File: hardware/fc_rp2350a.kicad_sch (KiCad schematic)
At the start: 51 parts, among them Q1 AP1606, Q2 AP1606, U1 TS2306A 240GF MSM 9_C2976675, U2 RP2354A, X1 XTM25012000JT00351001

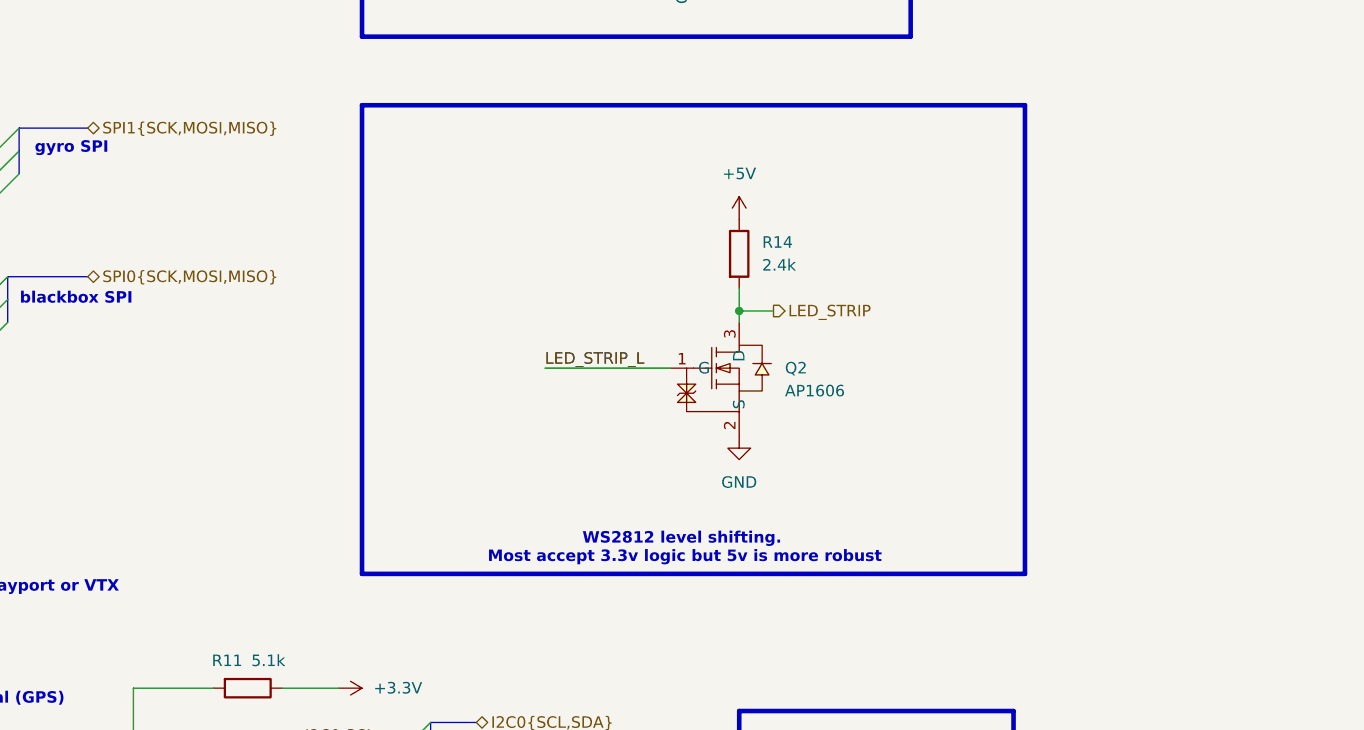
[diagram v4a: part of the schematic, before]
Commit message: LED strip: TXU0101 non-inverting stage replaces Q2/R14 (FB6 item 1, FW1)
Betaflight's RP2350 WS2812 driver cannot invert, so the inverting AP1606
open-drain stage (Q2 + R14 2.4k to +5V) is replaced by the OpenFC circuit:
GPIO8 /RP2354A/LED_STRIP_L -> U26 TXU0101DRYR (TI, SON-6 DRY) A -> BY ->
R115 200R 0201 (UNI-ROYAL 0201WMF2000TEE) -> LED_STRIP (LGA pad 46 ->
J20/J21/J31/J32). VCCA = Core +3.3V, VCCB = OE = +5V (as OpenFC U10; ds p19:
OE may be referenced to VCCA or VCCB, low/floating = Hi-Z). Bypass 100n
0201 GRM033R61E104KE14D on VCCA (C108) and VCCB (C109), ds p25.
Symbol, footprint and 3D model copied from ref-OpenFC into the project
libs (no silk; TI DRY0006A land; stencil 1:1 per ds p37 -> local paste
margin 0; courtyard on the body).

Core layout (F.Cu only, B.Cu still LGA only):
- U26 at the Q2/R14 slot (112.47,60.135) rot 270: A, GND and VCCA escape
  through three vias in the U2 removed-pad band (LED_STRIP_L In2, GND,
  +3.3V In3 plane); BY -> R115 below; R115 -> J91.46 via on F.
- C14 is 1.35 mm (pad edge) from VCCA, so C108 is kept, at the nearest
  legal spot: under R11, +3.3V pad on R11.1 (about 2 mm from U26).
- C109 right of R7 on the +5V feed (channel -> y61.5 -> C109 -> existing
  +5V track to via 117.65,60.2). R14's +5V via chain removed.
- Net-(R7-Pad1) now R7.1 -> via -> In2 -> existing via at U1 pin 2
  (that via was dangling before).
- U1 (BOOTSEL switch) 0.30 mm down; SCL pull-up stub rerouted along
  y59.37/x114.75; GND stitch via moved to 114.42,59.95; J50 'GND' label
  0.8 mm down (still beside J50) to clear C108.

DRC Core 28 -> 27 errors (via_dangling only), Base 21 unchanged; parity
non-missing 70/7 unchanged; unconnected 0/0; ERC 31 unchanged (warnings
+12: pin types as OpenFC symbol, 0201 nickname as existing parts).
Courtyard warnings Core 127 -> 132. Base board untouched.

Co-Authored-By: Claude Opus 5.5 <noreply@anthropic.com>
Claude-Session: https://claude.ai/code/session_01KTp3FLjVXfXdWrkmr6af7d
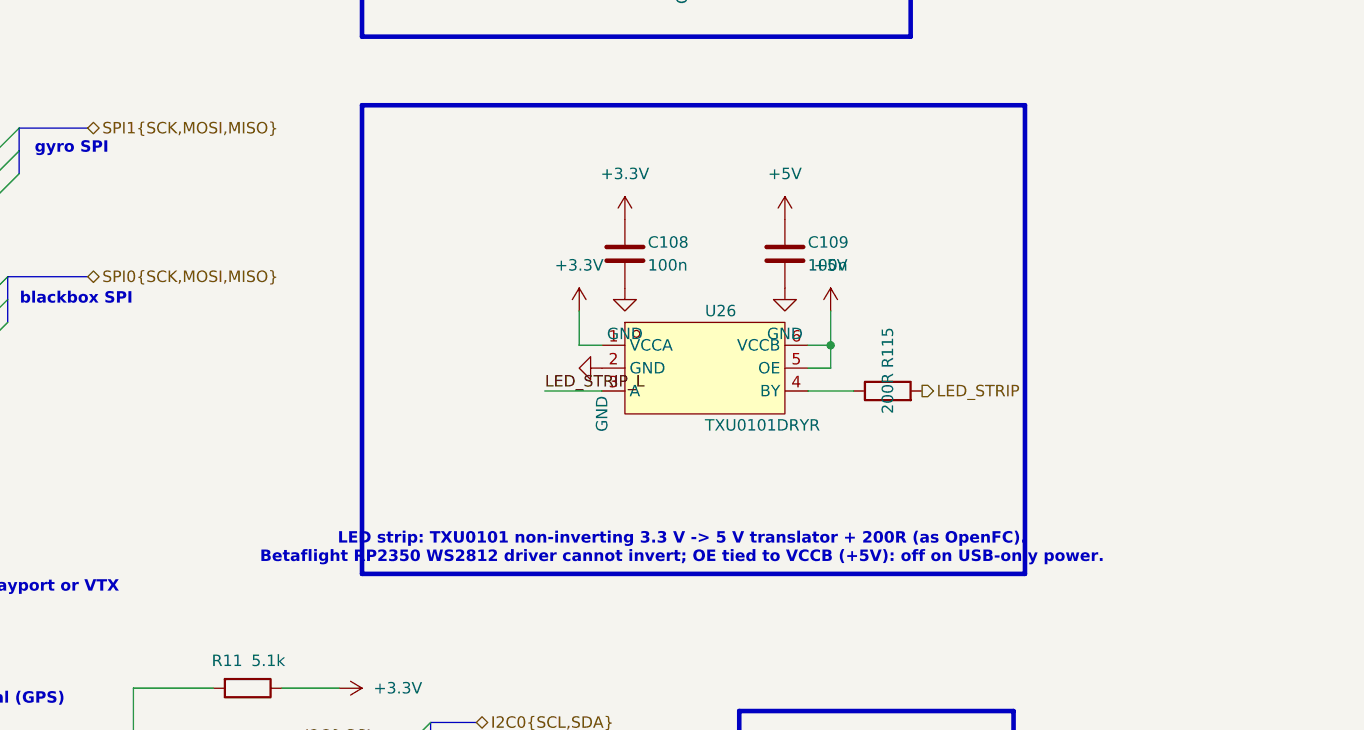
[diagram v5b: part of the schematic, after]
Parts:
- removed Q2: AP1606, lib:DFN-3L_L1.0-W0.6-P0.65-BR, symbol lib:DMN1150UFB-7B
- removed R14: 2.4k, Resistor_SMD:R_0201_0603Metric, symbol Device:R
- added C108, C109: 100n, Capacitor_SMD:C_0201_0603Metric, symbol Device:C
- added R115: 200R, Resistor_SMD:R_0201_0603Metric, symbol Device:R
- added U26: TXU0101DRYR, lib:SON-6_L1.5-W1.0-P0.50-TL, symbol lib:TXU0101DRYR
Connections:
- net +3.3V: now also C108.1, U26.1 (VCCA)
- net +5V: now also C109.1, U26.5 (OE), U26.6 (VCCB)
- net GND: now also C108.2, C109.2, U26.2 (GND)
- net LED_STRIP: now also R115.2
- net LED_STRIP_L: now also U26.3 (A)
- new net: R115.1, U26.4 (BY)
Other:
- note added: "LED strip: TXU0101 non-inverting 3.3 V -> 5 V translator + 200R (as OpenFC). Betaflight RP2350 WS2812 driver cannot invert; OE tied to VCCB (+5V): off on USB-only power."
- note removed: "WS2812 level shifting. Most accept 3.3v logic but 5v is more robust"

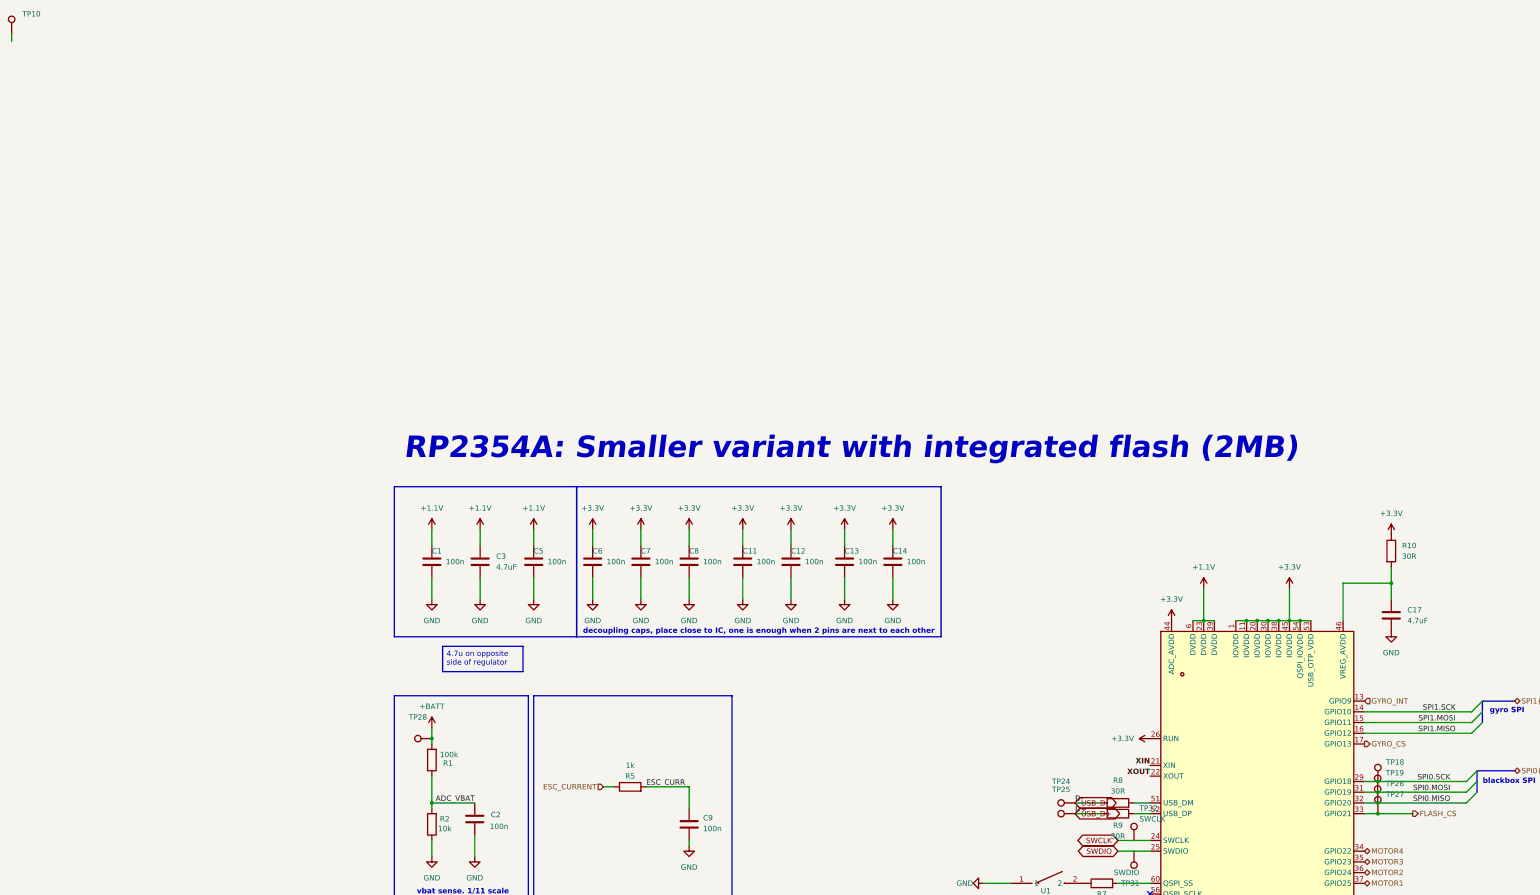
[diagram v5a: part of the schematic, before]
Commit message: One board: merge Base and Core onto the OpenAIO-Whoop 8L HDI stackup
- hardware/OpenAIO.kicad_pcb: the routed Base and Core layouts of 8fa8d7b
  side by side in one board, all routing kept (Core promoted to 8 layers
  before the append so no Base layer was dropped). J90/J91 LGA deleted;
  their 46 nets are now direct links (51 unconnected, listed in
  research/ROUTING.md). Stackup and board setup from OpenAIO-Whoop:
  8L HDI 1+6+1, 0.997 mm, 1 oz all layers, microvia 0.25/0.10,
  buried 0.33/0.15. Base DRC severities and exclusions kept.
- hardware/OpenAIO.kicad_dru: canonical block, Whoop HDI via rules,
  Base/Core rules that still apply; LGA, 2 oz and 1.6 mm via rules gone.
- Schematic: core_interface sheet removed; DPS368 baro U28 on I2C0;
  review fixes (U3 HF cap C116, RP2354 caps C117/C118, buzzer flyback D10,
  SD card on +3.3V, D9 on +4v5, FLASH_CS -> SD_CS, PWR_FLAGs, U7 pin
  names, ESC cap pin types, L4 LCSC). ERC 32 -> 0 errors.
- Libraries project-local: every footprint, 3D model and symbol in lib;
  OPENDRONE_LIB aliases removed from the lib tables.
- Two-board projects, multiboard config and LGA tools removed; Whoop
  board tools added in hardware/tools.
- Docs: README, AGENTS.md, research/ROUTING.md (hand-over),
  SCHEMATIC-REVIEW-2026-10-15.md, Betaflight target baro.

DRC: 38 errors (25 dangling LGA escape vias, 13 Core leftovers listed),
51 unconnected (the Base-Core links), 0 net or value parity issues.

Co-Authored-By: Claude Opus 5.5 <noreply@anthropic.com>
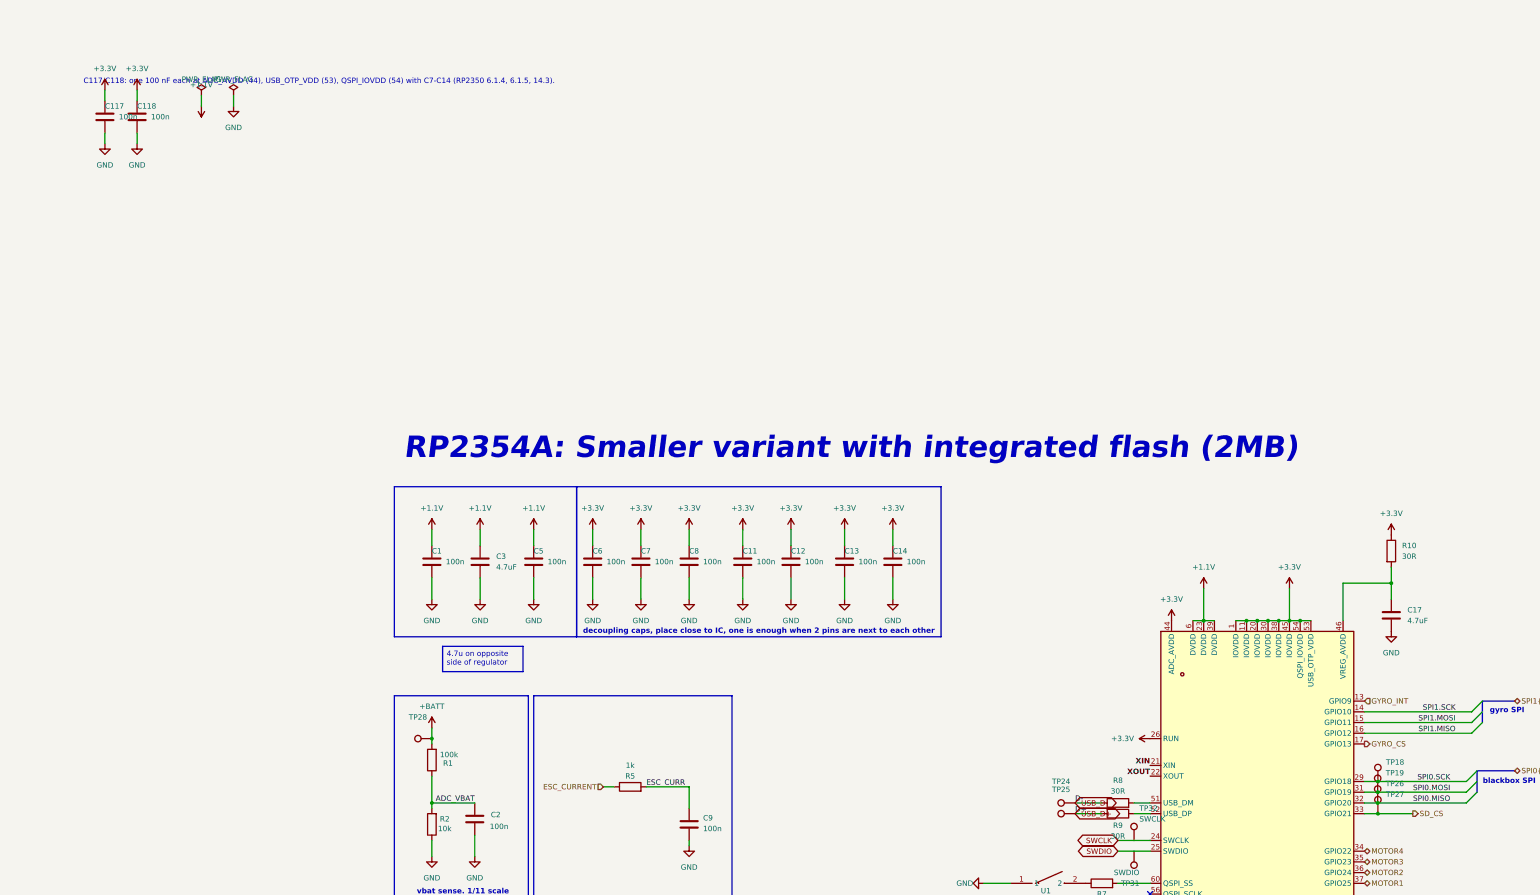
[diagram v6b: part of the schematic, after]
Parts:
- removed TP10: TestPoint, OpenDrone:TestPoint_Pad_D1.0mm, symbol Connector:TestPoint
- added C117, C118: 100n, lib:C_0201_0603Metric, symbol Device:C
- C1, C10, C108, C109, C11, C12, C13, C14, C2, C4, C5, C6, C7, C8, C9: footprint Capacitor_SMD:C_0201_0603Metric -> lib:C_0201_0603Metric
- C15, C16, C17, C3: footprint Capacitor_SMD:C_0402_1005Metric -> lib:C_0402_1005Metric
- D1: footprint LED_SMD:LED_0402_1005Metric -> lib:LED_0402_1005Metric
- R1, R10, R11, R115, R12, R13, R15, R16, R2, R3, R4, R5, R6, R7, R8, R9: footprint Resistor_SMD:R_0201_0603Metric -> lib:R_0201_0603Metric
- TP18, TP19, TP24, TP25, TP26, TP27, TP28: footprint TestPoint:TestPoint_Pad_D1.0mm -> lib:TestPoint_Pad_D1.0mm
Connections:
- net +3.3V: now also C117.1, C118.1
- net GND: now also C117.2, C118.2
- net FLASH_CS renamed SD_CS
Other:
- note added: "C117/C118: one 100 nF each at ADC_AVDD (44), USB_OTP_VDD (53), QSPI_IOVDD (54) with C7-C14 (RP2350 6.1.4, 6.1.5, 14.3)."

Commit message: One board from the owner's 2026-08-22 Base and Core, BMP580 baro (#26)
The board is rebuilt from d81e559 (the hand-routed Base recovered from KiCad
local history and the hand-routed Core of 1fe3d21) plus the always-on +10V of
9aba717, instead of the agent-reworked 8fa8d7b. Both layouts sit side by side
in hardware/OpenAIO.kicad_pcb with all routing kept (2513 tracks, 1577 vias),
on the OpenAIO-Whoop 8L HDI stackup.

- Schematic: Core_Interface (J90/J91 LGA) removed; U26 BMP580 + C107/C108 on
  I2C0 at 0x47 (Betaflight BMP5xx default). Netlist otherwise identical to
  9aba717; ERC 31 errors, the 9aba717 baseline.
- Board: Base netclasses and severities; rule area "Core layout" keeps the
  Core's 0.09 line standard. DRC: 3 errors (USB1 peg), 37 unconnected (links).
- lib.pretty footprints replaced by the board instances; BMP580 imported with
  easyeda2kicad (LCSC C22391138).
- Not carried from 8fa8d7b: TXU0101 LED-strip buffer, +3V3_ESC, SWD pads,
  DFM edits; firmware ISSUES I2/I3 reopened.
- Docs: README pinout re-measured, AGENTS.md, research/ROUTING.md, Betaflight
  target USE_BARO_BMP580.

Co-authored-by: Stan <stan@openaio.local>
Co-authored-by: Claude Opus 5.5 <noreply@anthropic.com>
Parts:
- removed C108, C109, C117, C118: 100n, lib:C_0201_0603Metric, symbol Device:C
- removed R115: 200R, lib:R_0201_0603Metric, symbol Device:R
- removed TP31: SWDIO, lib:TestPoint_Pad_D0.8mm, symbol Connector:TestPoint
- removed TP32: SWCLK, lib:TestPoint_Pad_D0.8mm, symbol Connector:TestPoint
- removed U26: TXU0101DRYR, lib:SON-6_L1.5-W1.0-P0.50-TL, symbol lib:TXU0101DRYR
- added Q2: AP1606, lib:DFN-3L_L1.0-W0.6-P0.65-BR, symbol lib:DMN1150UFB-7B
- added R14: 2.4k, lib:R_0201_0603Metric, symbol Device:R
- added TP10: TestPoint, lib:TestPoint_Pad_D1.0mm, symbol Connector:TestPoint
- R7: value 1k -> 10k; LCSC C270365 -> C106225; MPN 0201WMF1001TEE -> RC0201FR-0710KL; Manufacturer UNI-ROYAL -> YAGEO
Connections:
- net +5V: now also R14.1
- net GND: now also Q2.2 (S)
- net LED_STRIP: now also Q2.3 (D), R14.2
- net LED_STRIP_L: now also Q2.1 (G)
- net SD_CS renamed FLASH_CS
- net SWCLK: no longer names the net of U2.24 (SWCLK)
- net SWDIO: no longer names the net of U2.25 (SWDIO)
- no-connect marks 8 -> 10
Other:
- note added: "WS2812 level shifting. Most accept 3.3v logic but 5v is more robust"
- note removed: "C117/C118: one 100 nF each at ADC_AVDD (44), USB_OTP_VDD (53), QSPI_IOVDD (54) with C7-C14 (RP2350 6.1.4, 6.1.5, 14.3)."
- note removed: "LED strip: TXU0101 non-inverting 3.3 V -> 5 V translator + 200R (as OpenFC). Betaflight RP2350 WS2812 driver cannot invert; OE tied to VCCB (+5V): off on USB-only power."
- title: RP2354A flight controller -> (none)

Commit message: Library: every symbol, footprint and 3D model project-local (#28)
* Owner: board cleanup, Core placed on the board

Co-Authored-By: Claude Opus 5.5 <noreply@anthropic.com>

* Library: every symbol, footprint and 3D model project-local

- 3D models: 275 board model paths and 28 lib.pretty footprints pointed at
  KiCad's stock install or at ${OPENDRONE_LIB} (which this machine's KiCad sets
  to a path that does not exist, so 9 models were missing). All now resolve to
  ${KIPRJMOD}/lib.3dshapes; the three missing ones come from the repo's
  KiCad-Library submodule. .wrl replaced by the .step sibling where one exists.
- Symbols: the 14 stock symbols (Device, power, Connector, Connector_Generic,
  MCU_Espressif) copied into lib.kicad_sym from the schematic's own cache and
  relinked as lib:. Four lib symbols refreshed from the schematic (they still
  held the 8fa8d7b copies).
- Pruned: 11 unused footprints, 7 unused symbols, unreferenced model files.
- tools/localise_models.py and tools/localise_symbols.py keep it that way.
- Checks: board diff is model lines only; netlist identical; ERC 31 errors as
  before, lib_symbol_mismatch 9 -> 0.

Co-Authored-By: Claude Opus 5.5 <noreply@anthropic.com>

---------

Co-authored-by: Stan <stan@openaio.local>
Co-authored-by: Claude Opus 5.5 <noreply@anthropic.com>
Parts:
- C1, C10, C11, C12, C13, C14, C15, C16, C17, C2, C3, C4, C5, C6, C7, C8, C9: symbol Device:C -> lib:C
- D1: symbol Device:LED -> lib:LED
- R1, R10, R11, R12, R13, R14, R15, R16, R2, R3, R4, R5, R6, R7, R8, R9: symbol Device:R -> lib:R
- TP10, TP18, TP19, TP24, TP25, TP26, TP27, TP28: symbol Connector:TestPoint -> lib:TestPoint
